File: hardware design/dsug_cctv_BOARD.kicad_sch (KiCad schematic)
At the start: 50 parts, among them J1 Conn_02x05_Top_Bottom, J3 TYPEC-304-ACP16, Q1 MMBT3904, Q2 MMBT3904, SW1 TS-1187A-B-A-B, SW2 24_detent, SW3 SW_Push, U1 AMS1117-3.3, U13 RP2040, U2 W25Q128JVS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

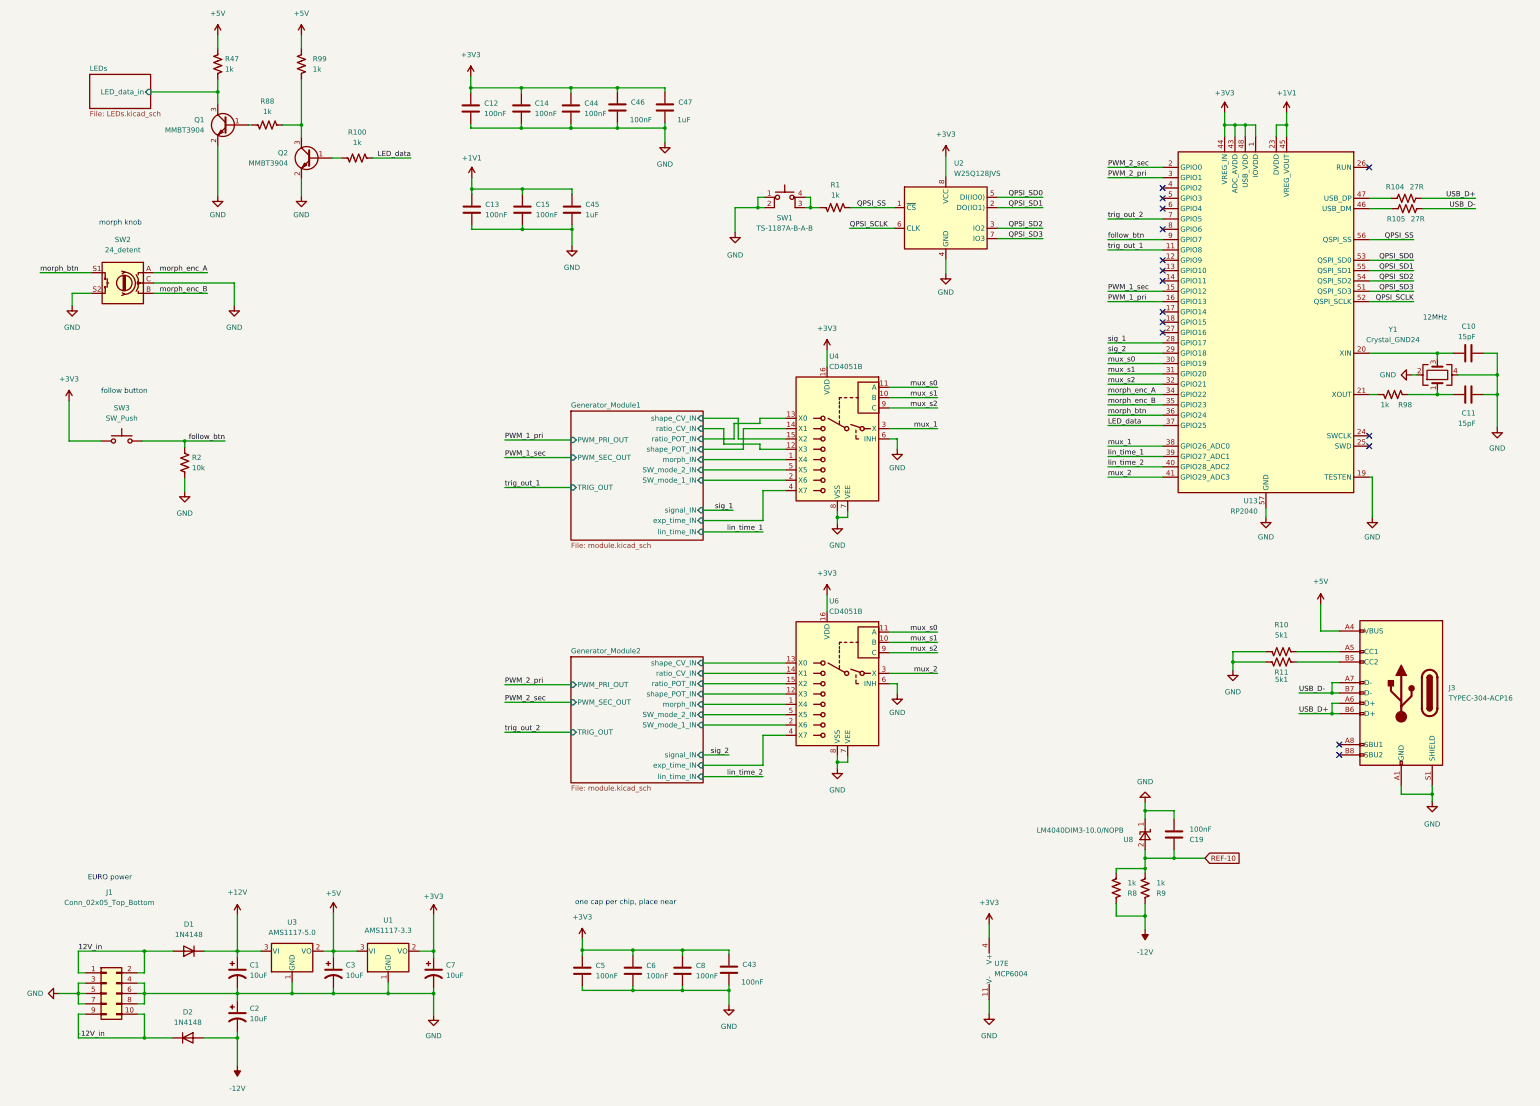
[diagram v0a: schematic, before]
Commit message: redid power circuitry
5V is now switching regulator, separate LDO for analog and digital
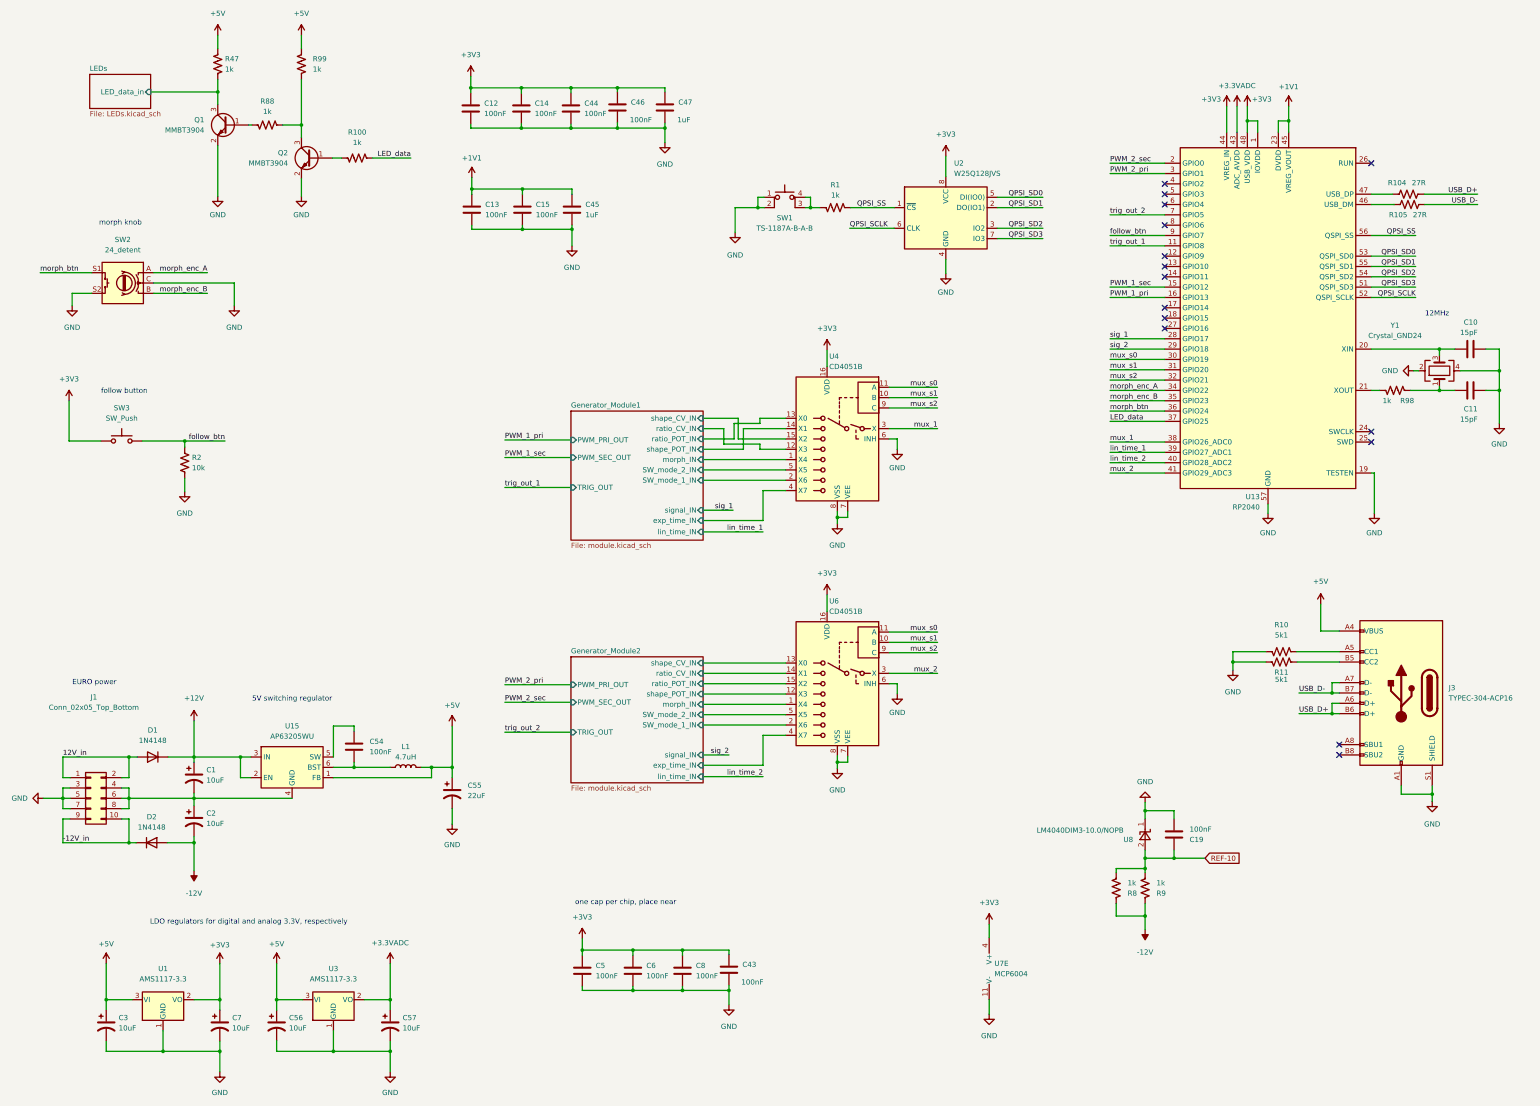
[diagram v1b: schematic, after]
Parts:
- removed U3: AMS1117-5.0, Package_TO_SOT_SMD:SOT-223-3_TabPin2, symbol Regulator_Linear:AMS1117-5.0
- added C54: 100nF, symbol Device:C
- added C55: 22uF, Capacitor_THT:CP_Radial_D5.0mm_P2.50mm, symbol Device:C_Polarized_US
- added C56, C57: 10uF, Capacitor_THT:CP_Radial_D5.0mm_P2.50mm, symbol Device:C_Polarized_US
- added L1: 4.7uH, symbol Device:L
- added U15: AP63205WU, Package_TO_SOT_SMD:TSOT-23-6, symbol Regulator_Switching:AP63205WU
- added U3: AMS1117-3.3, Package_TO_SOT_SMD:SOT-223-3_TabPin2, symbol Regulator_Linear:AMS1117-3.3
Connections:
- net +12V: now also U15.2 (EN), U15.3 (IN)
- net +3V3: no longer U13.43 (ADC_AVDD)
- net +5V: now also C55.1, C56.1, L1.2, U15.1 (FB), U3.3 (VI)
- net GND: now also C55.2, C56.2, C57.2, U3.1 (GND); no longer C1.2, C2.1, J1.4 (Pin_4), J1.6 (Pin_6), J1.8 (Pin_8)
- new net: C1.2, C2.1, J1.4 (Pin_4), J1.6 (Pin_6), J1.8 (Pin_8), U15.4 (GND)
- new net: C54.1, U15.5 (SW)
- new net: C54.2, L1.1, U15.6 (BST)
- new net +3.3VADC: C57.1, U13.43 (ADC_AVDD), U3.2 (VO)
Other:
- note added: "5V switching regulator"
- note added: "LDO regulators for digital and analog 3.3V, respectively"
- moved on the sheet: C1, C10, C11, C2, C3, C7, D1, D2, J1, R104, R105, R98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

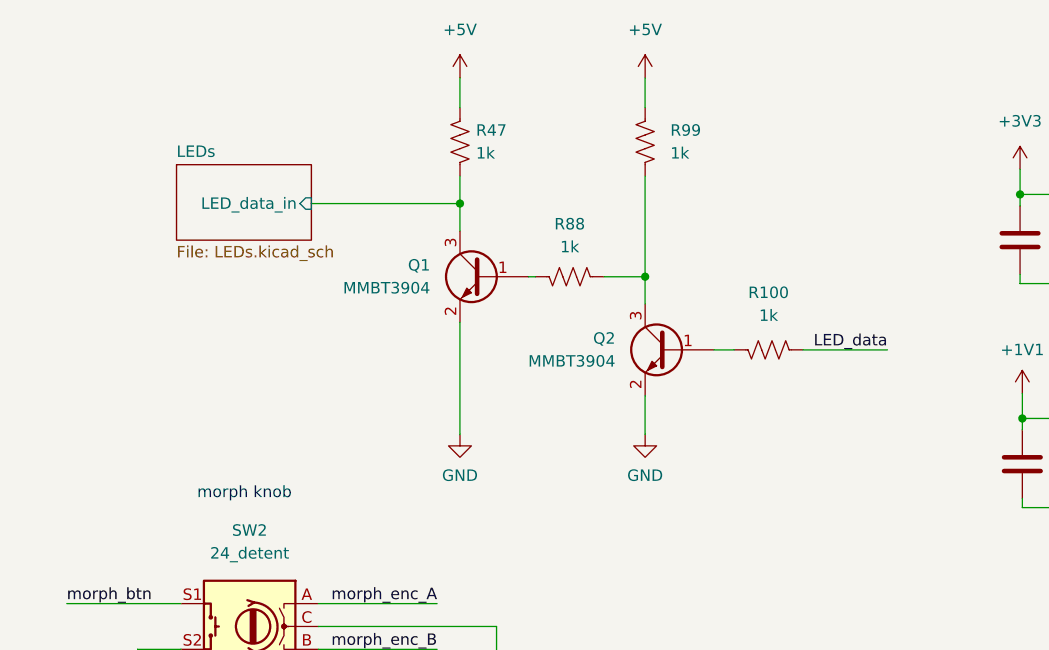
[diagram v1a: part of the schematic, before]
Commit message: upgraded led level shifter
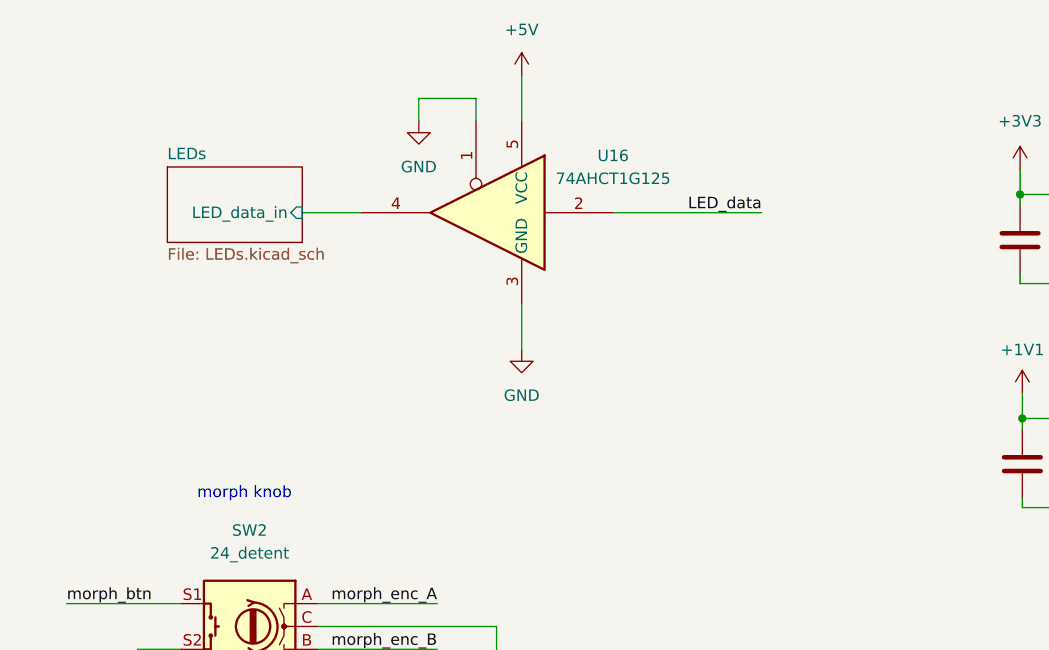
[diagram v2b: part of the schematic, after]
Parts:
- removed Q1, Q2: MMBT3904, Package_TO_SOT_SMD:SOT-23, symbol Transistor_BJT:MMBT3904
- removed R100, R47, R88, R99: 1k, Resistor_SMD:R_0603_1608Metric, symbol Device:R_US
- added U16: 74AHCT1G125, symbol 74xGxx:74AHCT1G125
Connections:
- net +5V: now also U16.5 (VCC)
- net GND: now also U16.1, U16.3 (GND)
- net LED_data: now also U16.2
- net LEDs/LED_data_in: now also U16.4

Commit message: fixing schematic issues, change output caps
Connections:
- net +3.3VADC: now also U7.4 (V+)
- net +3V3: no longer U7.4 (V+)
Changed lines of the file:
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@@
 	(wire
 		(pts
+			(xy 255.27 240.03) (xy 255.27 242.57)
+		)
+		(stroke
+			(width 0)
+			(type default)
+		)
+	)
+	(wire
+		(pts
 			(xy 184.912 177.546) (xy 205.232 177.546)
 		)
@@
 	(wire
 		(pts
-			(xy 255.27 239.268) (xy 255.27 242.57)
-		)
-		(stroke
-			(width 0)
-			(type default)
-		)
-	)
-	(wire
-		(pts
 			(xy 93.98 190.5) (xy 99.06 190.5)
 		)
@@
 	)
 	(symbol
+		(lib_id "power:+3.3VADC")
+		(at 255.27 240.03 0)
+		(unit 1)
+		(exclude_from_sim no)
+		(in_bom yes)
+		(on_board yes)
+		(dnp no)
+		(fields_autoplaced yes)
+		(property "Reference" "#PWR054"
+			(at 259.08 241.3 0)
+			(effects
+				(font
+					(size 1.27 1.27)
+				)
+				(hide yes)
+			)
+		)
+		(property "Value" "+3.3VADC"
+			(at 255.27 234.95 0)
+			(effects
+				(font
+					(size 1.27 1.27)
+				)
+			)
+		)
+		(property "Footprint" ""
+			(at 255.27 240.03 0)
+			(effects
+				(font
+					(size 1.27 1.27)
+				)
+				(hide yes)
+			)
+		)
+		(property "Datasheet" ""
+			(at 255.27 240.03 0)
+			(effects
+				(font
+					(size 1.27 1.27)
+				)
+				(hide yes)
+			)
+		)
+		(property "Description" "Power symbol creates a global label with name \"+3.3VADC\""
+			(at 255.27 240.03 0)
+			(effects
+				(font
+					(size 1.27 1.27)
+				)
+				(hide yes)
+			)
+		)
+		(pin "1"
+		)
+		(instances
+			(project "dsug_cctv_BOARD"
+				(path "/51d56f2e-5cbb-4b7a-b5cc-91fdc3a7308d"
+					(reference "#PWR054")
+					(unit 1)
+				)
+			)
+		)
+	)
+	(symbol
 		(lib_id "power:GND")
 		(at 232.664 182.626 0)
@@
 					(unit 1)
 				)
-			)
-		)
-	)
-	(symbol
-		(lib_id "power:+3V3")
-		(at 255.27 239.268 0)
-		(unit 1)
-		(exclude_from_sim no)
-		(in_bom yes)
-		(on_board yes)
-		(dnp no)
-		(fields_autoplaced yes)
-		(property "Reference" "#PWR0126"
-			(at 255.27 243.078 0)
-			(effects
-				(font
-					(size 1.27 1.27)
-				)
-				(hide yes)
-			)
-		)
-		(property "Value" "+3V3"
-			(at 255.27 233.934 0)
-			(effects
-				(font
-					(size 1.27 1.27)
-				)
-			)
-		)
-		(property "Footprint" ""
-			(at 255.27 239.268 0)
-			(effects
-				(font
-					(size 1.27 1.27)
-				)
-				(hide yes)
-			)
-		)
-		(property "Datasheet" ""
-			(at 255.27 239.268 0)
-			(effects
-				(font
-					(size 1.27 1.27)
-				)
-				(hide yes)
-			)
-		)
-		(property "Description" ""
-			(at 255.27 239.268 0)
-			(effects
-				(font
-					(size 1.27 1.27)
-				)
-				(hide yes)
-			)
-		)
-		(pin "1"
-		)
-		(instances
-			(project "dsug_cctv_BOARD"
-				(path "/51d56f2e-5cbb-4b7a-b5cc-91fdc3a7308d"
-					(reference "#PWR0126")
-					(unit 1)
-				)

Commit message: pcb rev2.5
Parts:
- removed C3: 10uF, Capacitor_THT:CP_Radial_D5.0mm_P2.50mm, symbol Device:C_Polarized_US
- added C16, C4, C58, C59: 100nF, Capacitor_SMD:C_0603_1608Metric, symbol Device:C
- C54: footprint (none) -> Capacitor_SMD:C_0603_1608Metric
- C55: value 22uF -> 10uF
- L1: footprint (none) -> Inductor_SMD:L_1206_3216Metric
- U16: footprint (none) -> Package_TO_SOT_SMD:SOT-23-5
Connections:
- net +3.3VADC: now also C16.1, C4.1, C58.1, C59.1
- net GND: now also C1.2, C2.1, J1.4 (Pin_4), J1.6 (Pin_6), J1.8 (Pin_8), U15.4 (GND), C16.2, C4.2, C58.2, C59.2
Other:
- moved on the sheet: C43, C5, C6, C8

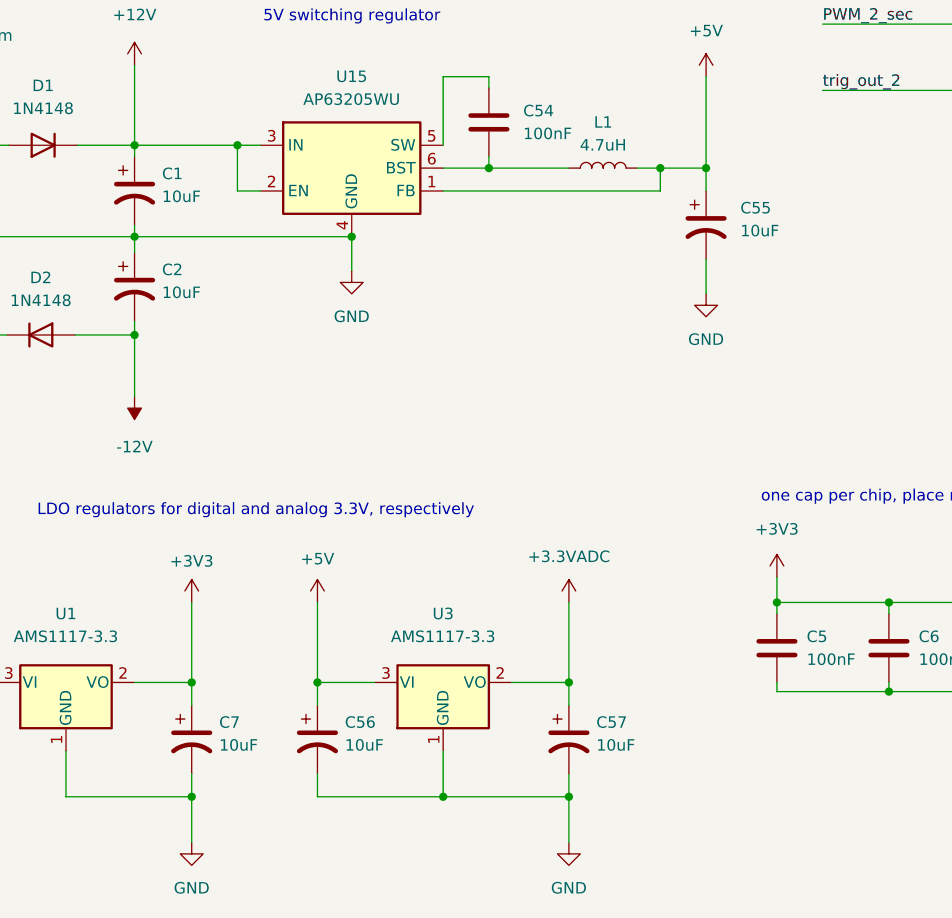
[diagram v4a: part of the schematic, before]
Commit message: swapped 10uF for 22uF caps
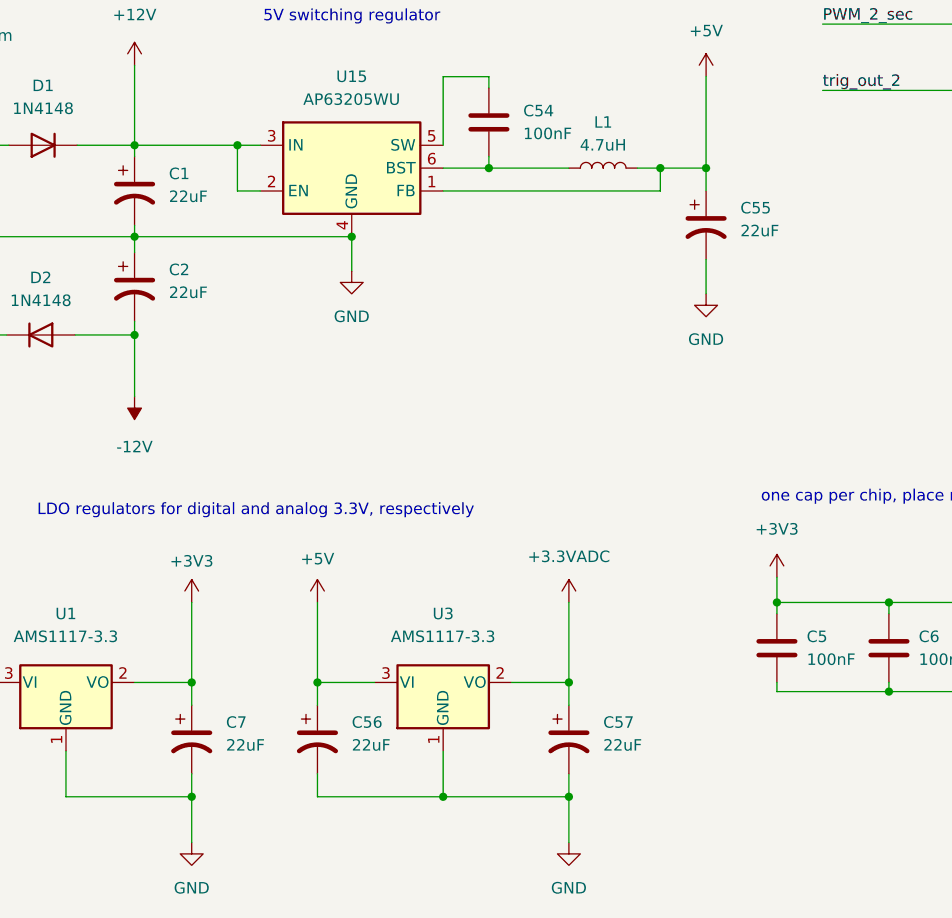
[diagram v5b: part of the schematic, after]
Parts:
- C1, C2, C55, C56, C57, C7: value 10uF -> 22uF
- L1: footprint Inductor_SMD:L_1206_3216Metric -> User_Footprints:L_TaiTech_HPC3010TF-4R7M
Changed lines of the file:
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@@
 		(fields_autoplaced yes)
 		(property "Reference" "C56"
-			(at 83.058 262.2549 0)
+			(at 83.82 262.2549 0)
 			(effects
 				(font
@@
 			)
 		)
-		(property "Value" "10uF"
-			(at 83.058 264.7949 0)
+		(property "Value" "22uF"
+			(at 83.82 264.7949 0)
 			(effects
 				(font
@@
 		(fields_autoplaced yes)
 		(property "Reference" "C7"
-			(at 69.088 262.2549 0)
+			(at 69.85 262.2549 0)
 			(effects
 				(font
@@
 			)
 		)
-		(property "Value" "10uF"
-			(at 69.088 264.7949 0)
+		(property "Value" "22uF"
+			(at 69.85 264.7949 0)
 			(effects
 				(font
@@
 			)
 		)
-		(property "Footprint" "Inductor_SMD:L_1206_3216Metric"
+		(property "Footprint" "User_Footprints:L_TaiTech_HPC3010TF-4R7M"
 			(at 111.76 200.66 0)
 			(effects
@@
 			)
 		)
-		(property "Value" "10uF"
+		(property "Value" "22uF"
 			(at 127 207.6449 0)
 			(effects
@@
 		(fields_autoplaced yes)
 		(property "Reference" "C1"
-			(at 62.738 201.2949 0)
+			(at 63.5 201.2949 0)
 			(effects
 				(font
@@
 			)
 		)
-		(property "Value" "10uF"
-			(at 62.738 203.8349 0)
+		(property "Value" "22uF"
+			(at 63.5 203.8349 0)
 			(effects
 				(font
@@
 		(fields_autoplaced yes)
 		(property "Reference" "C57"
-			(at 110.998 262.2549 0)
+			(at 111.76 262.2549 0)
 			(effects
 				(font
@@
 			)
 		)
-		(property "Value" "10uF"
-			(at 110.998 264.7949 0)
+		(property "Value" "22uF"
+			(at 111.76 264.7949 0)
 			(effects
 				(font
@@
 		(fields_autoplaced yes)
 		(property "Reference" "C2"
-			(at 62.738 211.9629 0)
+			(at 63.5 211.9629 0)
 			(effects
 				(font
@@
 			)
 		)
-		(property "Value" "10uF"
-			(at 62.738 214.5029 0)
+		(property "Value" "22uF"
+			(at 63.5 214.5029 0)
 			(effects
 				(font
